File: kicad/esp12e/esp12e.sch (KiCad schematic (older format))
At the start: 4 parts

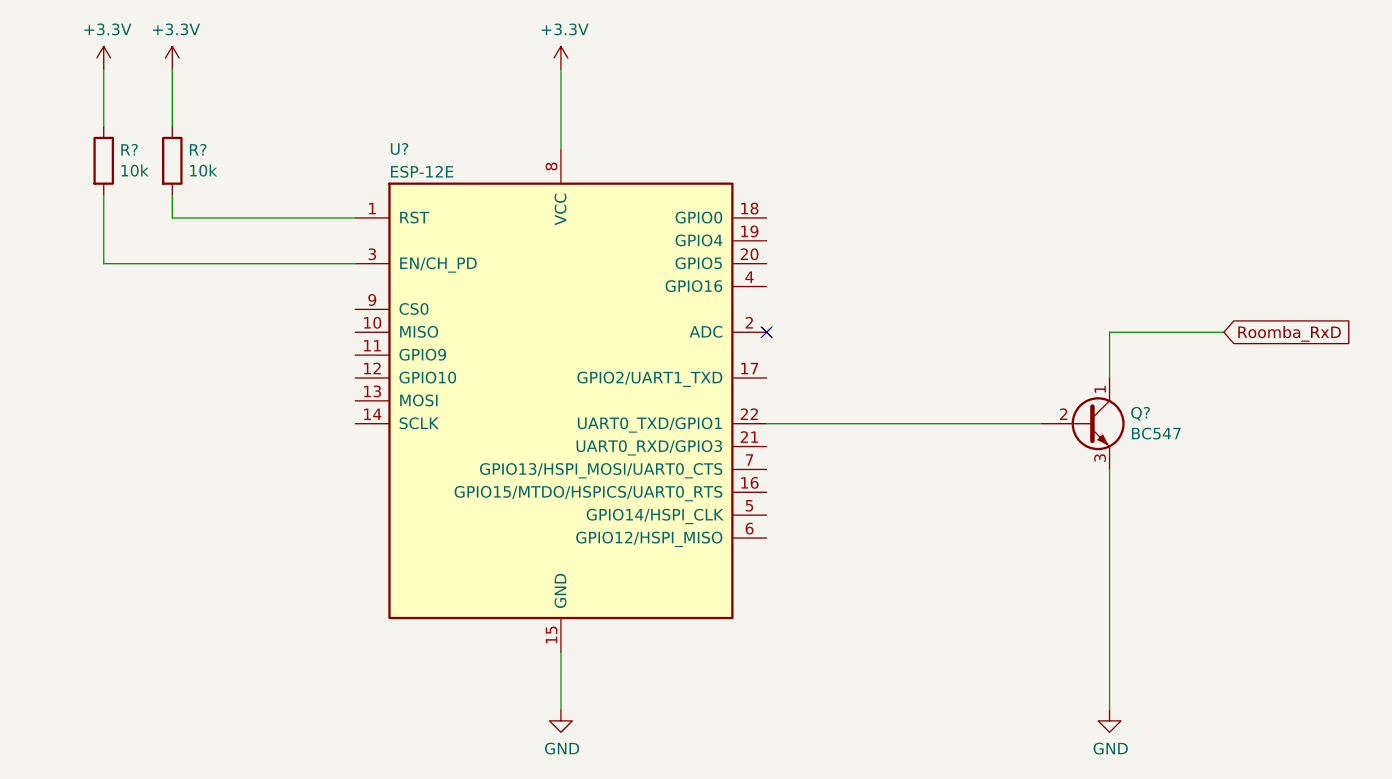
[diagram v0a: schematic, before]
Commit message: voltage regulator is missing in pcb
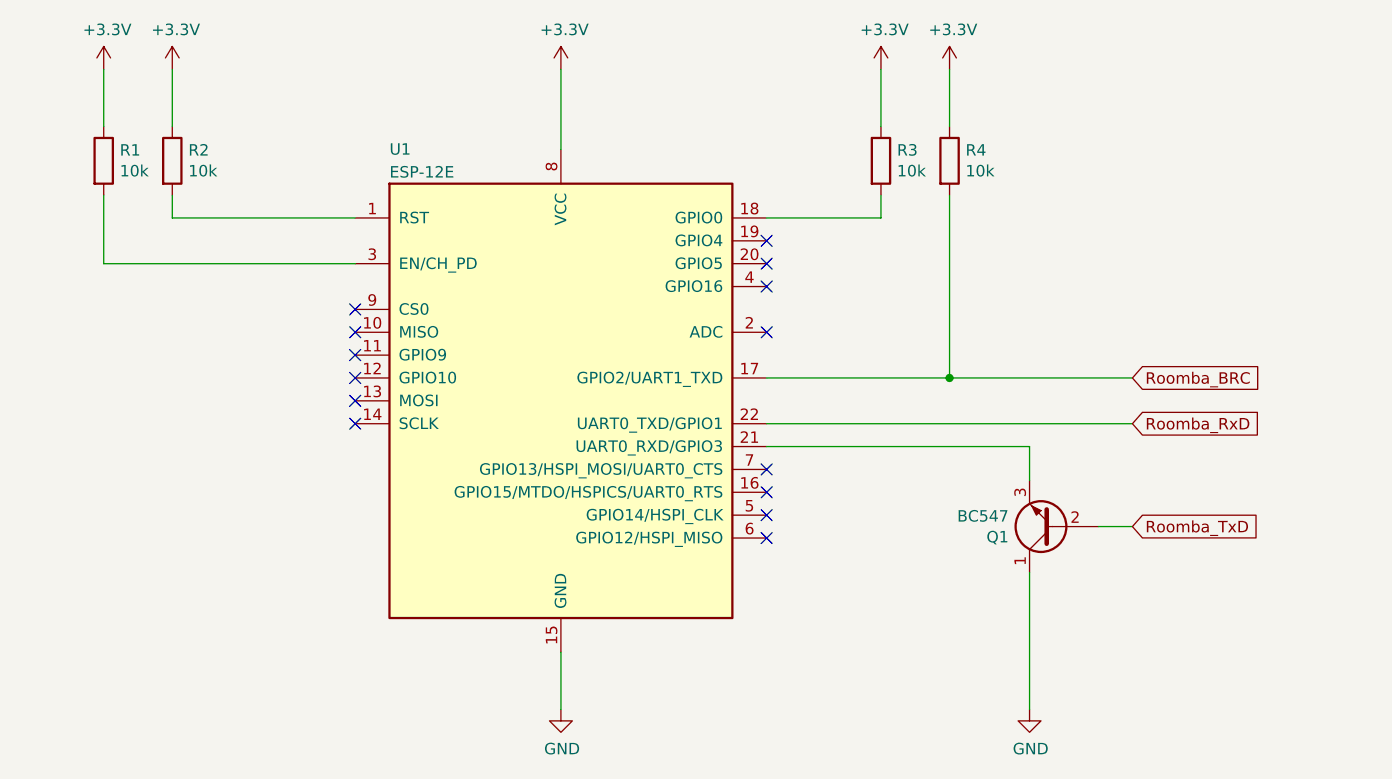
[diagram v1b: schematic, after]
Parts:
- added R3, R4: 10k, symbol Device:R
- gave numbers to parts that had none: 4
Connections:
- net +3V3: now also R3.1, R4.1
- net GND: now also Q1.1 (C); no longer Q1.3 (E)
- net Roomba_RxD: now also U1.22 (UART0_TXD/GPIO1); no longer Q1.1 (C)
- net Roomba_BRC: now reaches U1.17 (GPIO2/UART1_TXD)
- net Roomba_BRC: now also R4.2
- net at U1.18 (GPIO0): now also R3.2
- net at U1.21 (UART0_RXD/GPIO3): now also Q1.3 (E)
- net Roomba_TxD: now reaches Q1.2 (B)
- net Roomba_TxD: no longer U1.22 (UART0_TXD/GPIO1)
- no-connect marks 1 -> 14
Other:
- moved on the sheet: Q1
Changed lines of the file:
@@
 EESchema Schematic File Version 4
+LIBS:esp12e-cache
 EELAYER 26 0
 EELAYER END
@@
 $EndDescr
 $Comp
-L RF_Module:ESP-12E U?
+L RF_Module:ESP-12E U1
 U 1 1 5ABE583B
 P 5200 3800
-F 0 "U?" H 4450 4900 50  0000 L CNN
+F 0 "U1" H 4450 4900 50  0000 L CNN
 F 1 "ESP-12E" H 4450 4800 50  0000 L CNN
 F 2 "RF_Module:ESP-12E" H 5200 4050 50  0001 C CNN
@@
 $EndComp
 $Comp
-L power:GND #PWR?
+L power:GND #PWR04
 U 1 1 5ABE5A62
 P 5200 5150
-F 0 "#PWR?" H 5200 4900 50  0001 C CNN
+F 0 "#PWR04" H 5200 4900 50  0001 C CNN
 F 1 "GND" H 5205 4977 50  0000 C CNN
 F 2 "" H 5200 5150 50  0001 C CNN
@@
 $EndComp
 $Comp
-L Device:R R?
+L Device:R R2
 U 1 1 5ABE5AD5
 P 3500 2750
-F 0 "R?" H 3570 2796 50  0000 L CNN
+F 0 "R2" H 3570 2796 50  0000 L CNN
 F 1 "10k" H 3570 2705 50  0000 L CNN
 F 2 "" V 3430 2750 50  0001 C CNN
@@
 $EndComp
 $Comp
-L Device:R R?
+L Device:R R1
 U 1 1 5ABE5DD8
 P 3200 2750
-F 0 "R?" H 3270 2796 50  0000 L CNN
+F 0 "R1" H 3270 2796 50  0000 L CNN
 F 1 "10k" H 3270 2705 50  0000 L CNN
 F 2 "" V 3130 2750 50  0001 C CNN
@@
 	3200 3200 3200 2900
 $Comp
-L power:+3.3V #PWR?
+L power:+3.3V #PWR01
 U 1 1 5ABE6018
 P 3200 2350
-F 0 "#PWR?" H 3200 2200 50  0001 C CNN
+F 0 "#PWR01" H 3200 2200 50  0001 C CNN
 F 1 "+3.3V" H 3215 2523 50  0000 C CNN
 F 2 "" H 3200 2350 50  0001 C CNN
@@
 $EndComp
 $Comp
-L power:+3.3V #PWR?
+L power:+3.3V #PWR05
 U 1 1 5ABE6030
+P 6600 2350
+F 0 "#PWR05" H 6600 2200 50  0001 C CNN
+F 1 "+3.3V" H 6615 2523 50  0000 C CNN
+F 2 "" H 6600 2350 50  0001 C CNN
+F 3 "" H 6600 2350 50  0001 C CNN
+	1    6600 2350
+	1    0    0    -1
+$EndComp
+$Comp
+L power:+3.3V #PWR03
+U 1 1 5ABE6041
+P 5200 2350
+F 0 "#PWR03" H 5200 2200 50  0001 C CNN
+F 1 "+3.3V" H 5215 2523 50  0000 C CNN
+F 2 "" H 5200 2350 50  0001 C CNN
+F 3 "" H 5200 2350 50  0001 C CNN
+	1    5200 2350
+	1    0    0    -1
+$EndComp
+Wire Wire Line
+	5200 2350 5200 2700
+Wire Wire Line
+	6600 2600 6600 2350
+Wire Wire Line
+	3200 2350 3200 2600
+Wire Wire Line
+	5200 4900 5200 5150
+$Comp
+L Transistor_BJT:BC547 Q1
+U 1 1 5ABE6211
+P 7350 4350
+F 0 "Q1" H 7541 4396 50  0000 L CNN
+F 1 "BC547" H 7541 4305 50  0000 L CNN
+F 2 "Package_TO_SOT_THT:TO-92_Inline" H 7550 4275 50  0001 L CIN
+F 3 "http://www.fairchildsemi.com/ds/BC/BC547.pdf" H 7350 4350 50  0001 L CNN
+	1    7350 4350
+	-1   0    0    1
+$EndComp
+$Comp
+L power:GND #PWR07
+U 1 1 5ABE6324
+P 7250 5150
+F 0 "#PWR07" H 7250 4900 50  0001 C CNN
+F 1 "GND" H 7255 4977 50  0000 C CNN
+F 2 "" H 7250 5150 50  0001 C CNN
+F 3 "" H 7250 5150 50  0001 C CNN
+	1    7250 5150
+	1    0    0    -1
+$EndComp
+Text GLabel 7700 3900 2    50   Input ~ 0
+Roomba_RxD
+NoConn ~ 6100 3500
+NoConn ~ 6100 4400
+NoConn ~ 6100 4300
+NoConn ~ 6100 4100
+NoConn ~ 6100 4200
+NoConn ~ 6100 3100
+NoConn ~ 6100 3200
+NoConn ~ 6100 3300
+NoConn ~ 4300 3900
+NoConn ~ 4300 3800
+NoConn ~ 4300 3700
+NoConn ~ 4300 3600
+NoConn ~ 4300 3500
+NoConn ~ 4300 3400
+Wire Wire Line
+	6100 3900 7700 3900
+Text GLabel 7700 4350 2    50   Input ~ 0
+Roomba_TxD
+Wire Wire Line
+	7250 4150 7250 4000
+Wire Wire Line
+	7250 4000 6100 4000
+Wire Wire Line
+	7700 4350 7550 4350
+Wire Wire Line
+	7250 5150 7250 4550
+$Comp
+L Device:R R3
+U 1 1 5ABE698D
+P 6600 2750
+F 0 "R3" H 6670 2796 50  0000 L CNN
+F 1 "10k" H 6670 2705 50  0000 L CNN
+F 2 "" V 6530 2750 50  0001 C CNN
+F 3 "~" H 6600 2750 50  0001 C CNN
+	1    6600 2750
+	1    0    0    -1
+$EndComp
+$Comp
+L power:+3.3V #PWR02
+U 1 1 5ABE6B72
 P 3500 2350
-F 0 "#PWR?" H 3500 2200 50  0001 C CNN
+F 0 "#PWR02" H 3500 2200 50  0001 C CNN
 F 1 "+3.3V" H 3515 2523 50  0000 C CNN
 F 2 "" H 3500 2350 50  0001 C CNN
@@
 	1    0    0    -1
 $EndComp
-$Comp
-L power:+3.3V #PWR?
-U 1 1 5ABE6041
-P 5200 2350
-F 0 "#PWR?" H 5200 2200 50  0001 C CNN
-F 1 "+3.3V" H 5215 2523 50  0000 C CNN
-F 2 "" H 5200 2350 50  0001 C CNN
-F 3 "" H 5200 2350 50  0001 C CNN
-	1    5200 2350
-	1    0    0    -1
-$EndComp
-Wire Wire Line
-	5200 2350 5200 2700
 Wire Wire Line
 	3500 2600 3500 2350
 Wire Wire Line
-	3200 2350 3200 2600
-Wire Wire Line
-	5200 4900 5200 5150
-$Comp
-L Transistor_BJT:BC547 Q?
-U 1 1 5ABE6211
-P 7500 3900
-F 0 "Q?" H 7691 3946 50  0000 L CNN
-F 1 "BC547" H 7691 3855 50  0000 L CNN
-F 2 "Package_TO_SOT_THT:TO-92_Inline" H 7700 3825 50  0001 L CIN
-F 3 "http://www.fairchildsemi.com/ds/BC/BC547.pdf" H 7500 3900 50  0001 L CNN
-	1    7500 3900
-	1    0    0    -1
-$EndComp
-Wire Wire Line
-	7300 3900 6100 3900
-$Comp
-L power:GND #PWR?
-U 1 1 5ABE6324
-P 7600 5150
-F 0 "#PWR?" H 7600 4900 50  0001 C CNN
-F 1 "GND" H 7605 4977 50  0000 C CNN
-F 2 "" H 7600 5150 50  0001 C CNN
-F 3 "" H 7600 5150 50  0001 C CNN
-	1    7600 5150
-	1    0    0    -1
-$EndComp
-Wire Wire Line
-	7600 5150 7600 4100
-Text GLabel 8100 3500 2    50   Input ~ 0
-Roomba_RxD
-Wire Wire Line
-	7600 3500 7600 3700
-Wire Wire Line
-	7600 3500 8100 3500
-NoConn ~ 6100 3500
+	6100 3000 6600 3000
+Wire Wire Line
+	6600 3000 6600 2900
+$Comp
+L power:+3.3V #PWR06
+U 1 1 5ABE6DD0
+P 6900 2350
+F 0 "#PWR06" H 6900 2200 50  0001 C CNN
+F 1 "+3.3V" H 6915 2523 50  0000 C CNN
+F 2 "" H 6900 2350 50  0001 C CNN
+F 3 "" H 6900 2350 50  0001 C CNN
+	1    6900 2350
+	1    0    0    -1
+$EndComp
+Wire Wire Line
+	6900 2600 6900 2350
+$Comp
+L Device:R R4
+U 1 1 5ABE6DD7
+P 6900 2750
+F 0 "R4" H 6970 2796 50  0000 L CNN
+F 1 "10k" H 6970 2705 50  0000 L CNN
+F 2 "" V 6830 2750 50  0001 C CNN
+F 3 "~" H 6900 2750 50  0001 C CNN
+	1    6900 2750
+	1    0    0    -1
+$EndComp
+Wire Wire Line
+	6100 3700 6900 3700
+Wire Wire Line
+	6900 2900 6900 3700
+Text GLabel 7700 3700 2    50   Input ~ 0
+Roomba_BRC
+Wire Wire Line
+	7700 3700 6900 3700
+Connection ~ 6900 3700
 $EndSCHEMATC

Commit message: schematic complete
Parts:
- added U?: TSR_1-2433, Converters_DCDC_ACDC:DCDC-Conv_TRACO_TSR-1, symbol Regulator_Switching:TSR_1-2433
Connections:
- net +3V3: now also U?.3 (Vout)
- net GND: now also U?.2 (GND)
- new net Roomba_VCC: U?.1 (Vin)
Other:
- moved on the sheet: Q1, R1, R3, R4, U1
